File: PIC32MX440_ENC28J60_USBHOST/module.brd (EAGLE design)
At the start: 78.4 x 68.6 mm, 79 parts, among them IC1 IC_USBLC6-2, IC2 LM1117IMPX-3.3, IC4 ENC28J60, IC5 PIC32MX440FH, T1 BC847, U1 USD-SOCKETUSD, X1 22-23-2021, X2 CRYSTALS-NOGND-CFPX-217, X3 KUSBVX, X5 22-23-2021, Y1 CRYSTAL-GROUNDEDSMD-5X3.2, Y2 CRYSTAL-GROUNDEDSMD-5X3.2

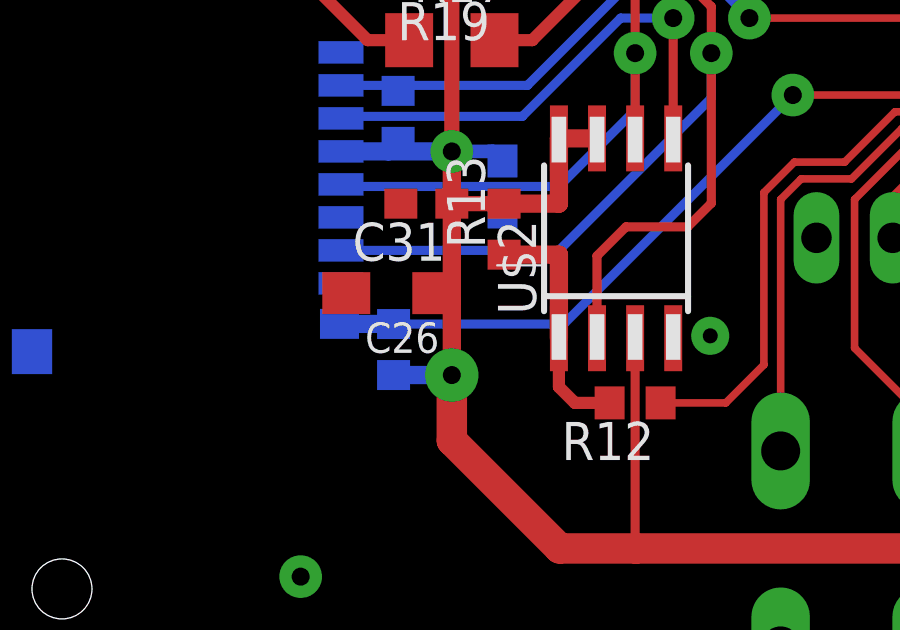
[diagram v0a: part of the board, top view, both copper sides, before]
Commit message: MISO pull-ups added
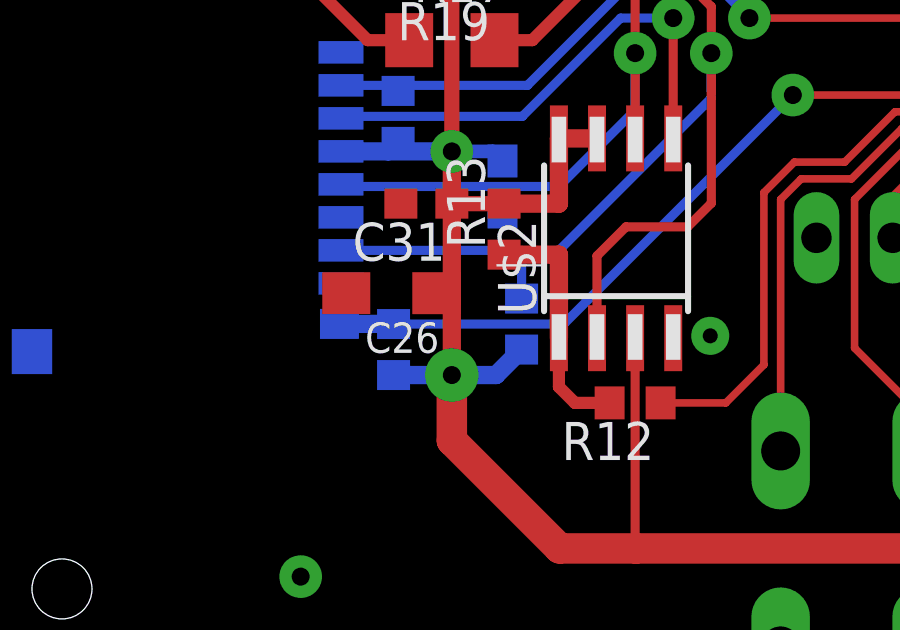
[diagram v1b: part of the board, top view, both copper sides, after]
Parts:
- added R22: (no value), rcl:R0603
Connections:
- net 3V_IN: now also R22.2
- net MISO: now also R22.1
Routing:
- net 3V_IN: track 190.1 -> 192.8 mm
- net MISO: track 55.9 -> 57.5 mm
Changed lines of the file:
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@@
 <element name="JP4" library="mw" package="2X05" value="" x="53.3908" y="9.525" rot="MR0"/>
 <element name="R15" library="rcl" package="R0805" value="" x="45.466" y="15.0876" rot="R90"/>
+<element name="R22" library="rcl" package="R0603" value="" x="20.32" y="13.8294" rot="MR270"/>
 </elements>
 <signals>
@@
 <wire x1="45.466" y1="14.1376" x2="45.466" y2="6.604" width="0.8128" layer="1"/>
 <wire x1="45.466" y1="6.604" x2="45.72" y2="6.35" width="0.6096" layer="1"/>
+<contactref element="R22" pad="2"/>
+<wire x1="17.995" y1="12.1294" x2="19.47" y2="12.1294" width="0.6096" layer="16"/>
+<wire x1="19.47" y1="12.1294" x2="20.32" y2="12.9794" width="0.6096" layer="16"/>
 </signal>
 <signal name="3V">
@@
 <wire x1="26.6446" y1="22.86" x2="26.6446" y2="17.8562" width="0.3048" layer="1"/>
 <wire x1="26.6446" y1="17.8562" x2="25.8572" y2="17.0688" width="0.3048" layer="1"/>
-<wire x1="14.3" y1="16.285" x2="21.5682" y2="16.285" width="0.3048" layer="16"/>
+<wire x1="14.3" y1="16.285" x2="20.32" y2="16.285" width="0.3048" layer="16"/>
+<wire x1="20.32" y1="16.285" x2="21.5682" y2="16.285" width="0.3048" layer="16"/>
 <wire x1="26.6446" y1="21.59" x2="26.6446" y2="22.86" width="0.3048" layer="16"/>
 <wire x1="21.5682" y1="16.285" x2="26.6446" y2="21.3614" width="0.3048" layer="16"/>
@@
 <wire x1="42.8918" y1="32.611" x2="34.7192" y2="32.611" width="0.254" layer="1"/>
 <wire x1="34.7192" y1="32.611" x2="33.3756" y2="31.2674" width="0.254" layer="1"/>
+<contactref element="R22" pad="1"/>
+<wire x1="20.32" y1="14.6794" x2="20.32" y2="16.285" width="0.3048" layer="16"/>
 </signal>
 <signal name="MOSI">
